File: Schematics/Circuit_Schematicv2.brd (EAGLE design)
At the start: 139.1 x 33.1 mm, 74 parts, among them Q2 LE33CZ

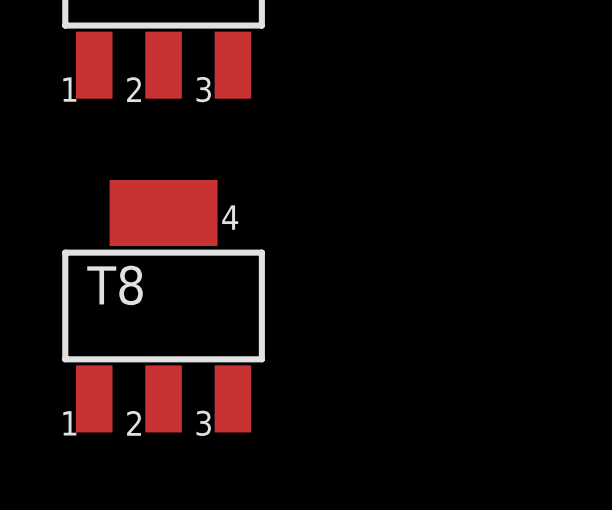
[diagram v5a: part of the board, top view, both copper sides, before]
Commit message: Final hardware changes and removed serial monitor from esp code in attempt to reduce noise
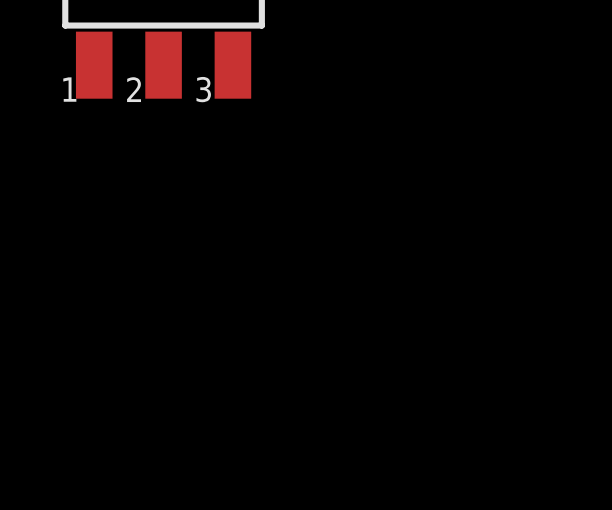
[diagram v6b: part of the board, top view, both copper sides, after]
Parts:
- removed T8: (no value), zetex:SOT223
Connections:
- removed net FAV3_GATE: MDL1.11, T8.1
- new net ESP_GPIO0: MDL1.12, R5.2, S2.2
- net FAV3: no longer T8.2, T8.4
- net GND: no longer T8.3
- net PREVIOUS_GATE: now also MDL1.11; no longer MDL1.12, R5.2, S2.2
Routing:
- net PREVIOUS_GATE: track 23.2 -> 0.00 mm, vias 2 -> 0
- net ESP_GPIO0: track 0.00 -> 23.2 mm, vias 0 -> 2
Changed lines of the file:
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@@
 <attribute name="OC_FARNELL" value="unknown" x="-85.8266" y="-64.135" size="1.778" layer="27" display="off"/>
-</element>
-<element name="T8" library="zetex" package="SOT223" value="" x="-85.8266" y="-75.2602">
-<attribute name="MF" value="" x="-85.8266" y="-75.2602" size="1.778" layer="27" display="off"/>
-<attribute name="OC_NEWARK" value="unknown" x="-85.8266" y="-75.2602" size="1.778" layer="27" display="off"/>
-<attribute name="MPN" value="" x="-85.8266" y="-75.2602" size="1.778" layer="27" display="off"/>
-<attribute name="OC_FARNELL" value="unknown" x="-85.8266" y="-75.2602" size="1.778" layer="27" display="off"/>
 </element>
 </elements>
@@
 <contactref element="T6" pad="3"/>
 <contactref element="T7" pad="3"/>
-<contactref element="T8" pad="3"/>
-<wire x1="-83.5152" y1="-67.2338" x2="-83.5152" y2="-78.359" width="0" layer="19" extent="1-1"/>
 <wire x1="-83.5152" y1="-56.1086" x2="-83.5152" y2="-67.2338" width="0" layer="19" extent="1-1"/>
 <wire x1="-83.5152" y1="-44.9834" x2="-83.5152" y2="-56.1086" width="0" layer="19" extent="1-1"/>
@@
 <wire x1="-2.3368" y1="25.527" x2="-1.524" y2="26.3398" width="0.2032" layer="16"/>
 <wire x1="-10.42035" y1="27.99715" x2="-11.7475" y2="26.67" width="0.2032" layer="1"/>
-<contactref element="T8" pad="4"/>
-<contactref element="T8" pad="2"/>
-<wire x1="-85.8266" y1="-72.1612" x2="-85.8266" y2="-78.359" width="0" layer="19" extent="1-1"/>
-<wire x1="-64.61125" y1="18.415" x2="-85.8266" y2="-72.1612" width="0" layer="19" extent="1-1"/>
 </signal>
 <signal name="FAV1">
@@
 <signal name="PREVIOUS_GATE">
 <contactref element="T2" pad="1"/>
+<contactref element="MDL1" pad="11"/>
+<wire x1="30.765" y1="28.25" x2="-88.138" y2="-11.6078" width="0" layer="19" extent="1-1"/>
+</signal>
+<signal name="VOLUP_GATE">
+<contactref element="T3" pad="1"/>
+<contactref element="MDL1" pad="14"/>
+<wire x1="36.765" y1="28.25" x2="-88.138" y2="-22.733" width="0" layer="19" extent="1-1"/>
+</signal>
+<signal name="VOLDOWN_GATE">
+<contactref element="T4" pad="1"/>
+<contactref element="MDL1" pad="13"/>
+<wire x1="34.765" y1="28.25" x2="-88.138" y2="-33.8582" width="0" layer="19" extent="1-1"/>
+</signal>
+<signal name="MUTE_GATE">
+<contactref element="T5" pad="1"/>
+<contactref element="MDL1" pad="5"/>
+<wire x1="32.765" y1="44.45" x2="-88.138" y2="-44.9834" width="0" layer="19" extent="1-1"/>
+</signal>
+<signal name="FAV1_GATE">
+<contactref element="T6" pad="1"/>
+<contactref element="MDL1" pad="4"/>
+<wire x1="34.765" y1="44.45" x2="-88.138" y2="-56.1086" width="0" layer="19" extent="1-1"/>
+</signal>
+<signal name="FAV2_GATE">
+<contactref element="T7" pad="1"/>
+<contactref element="MDL1" pad="7"/>
+<wire x1="28.765" y1="44.45" x2="-88.138" y2="-67.2338" width="0" layer="19" extent="1-1"/>
+</signal>
+<signal name="ESP_GPIO0">
 <contactref element="MDL1" pad="12"/>
 <contactref element="R5" pad="2"/>
@@
 <via x="32.86125" y="26.51125" extent="1-16" drill="0.6096"/>
 <via x="44.45" y="26.51125" extent="1-16" drill="0.6096"/>
-<wire x1="32.86125" y1="26.51125" x2="-88.138" y2="-11.6078" width="0" layer="19" extent="1-1"/>
-</signal>
-<signal name="VOLUP_GATE">
-<contactref element="T3" pad="1"/>
-<contactref element="MDL1" pad="14"/>
-<wire x1="36.765" y1="28.25" x2="-88.138" y2="-22.733" width="0" layer="19" extent="1-1"/>
-</signal>
-<signal name="VOLDOWN_GATE">
-<contactref element="T4" pad="1"/>
-<contactref element="MDL1" pad="13"/>
-<wire x1="34.765" y1="28.25" x2="-88.138" y2="-33.8582" width="0" layer="19" extent="1-1"/>
-</signal>
-<signal name="MUTE_GATE">
-<contactref element="T5" pad="1"/>
-<contactref element="MDL1" pad="5"/>
-<wire x1="32.765" y1="44.45" x2="-88.138" y2="-44.9834" width="0" layer="19" extent="1-1"/>
-</signal>
-<signal name="FAV1_GATE">
-<contactref element="T6" pad="1"/>
-<contactref element="MDL1" pad="4"/>
-<wire x1="34.765" y1="44.45" x2="-88.138" y2="-56.1086" width="0" layer="19" extent="1-1"/>
-</signal>
-<signal name="FAV2_GATE">
-<contactref element="T7" pad="1"/>
-<contactref element="MDL1" pad="7"/>
-<wire x1="28.765" y1="44.45" x2="-88.138" y2="-67.2338" width="0" layer="19" extent="1-1"/>
-</signal>
-<signal name="FAV3_GATE">
-<contactref element="T8" pad="1"/>
-<contactref element="MDL1" pad="11"/>
-<wire x1="30.765" y1="28.25" x2="-88.138" y2="-78.359" width="0" layer="19" extent="1-1"/>
 </signal>
 </signals>

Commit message: Updated the PS for the PIC
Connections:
- removed net N$1: U$1.19, U$1.57
- net 3.3V: now also U$1.19, U$1.57
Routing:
- net N$1: track 13.2 -> 0.00 mm
- net 3.3V: track 279.1 -> 292.3 mm
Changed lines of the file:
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@@
 <?xml version="1.0" encoding="utf-8"?>
 <!DOCTYPE eagle SYSTEM "eagle.dtd">
-<eagle version="8.0.0">
+<eagle version="8.1.0">
 <drawing>
 <settings>
@@
 <element name="T1" library="zetex" package="SOT223" value="" x="-85.8266" y="2.6162">
 <attribute name="MF" value="" x="-85.8266" y="2.6162" size="1.778" layer="27" display="off"/>
-<attribute name="OC_NEWARK" value="unknown" x="-85.8266" y="2.6162" size="1.778" layer="27" display="off"/>
 <attribute name="MPN" value="" x="-85.8266" y="2.6162" size="1.778" layer="27" display="off"/>
 <attribute name="OC_FARNELL" value="unknown" x="-85.8266" y="2.6162" size="1.778" layer="27" display="off"/>
+<attribute name="OC_NEWARK" value="unknown" x="-85.8266" y="2.6162" size="1.778" layer="27" display="off"/>
 </element>
 <element name="T2" library="zetex" package="SOT223" value="" x="-85.8266" y="-8.509">
 <attribute name="MF" value="" x="-85.8266" y="-8.509" size="1.778" layer="27" display="off"/>
-<attribute name="OC_NEWARK" value="unknown" x="-85.8266" y="-8.509" size="1.778" layer="27" display="off"/>
 <attribute name="MPN" value="" x="-85.8266" y="-8.509" size="1.778" layer="27" display="off"/>
 <attribute name="OC_FARNELL" value="unknown" x="-85.8266" y="-8.509" size="1.778" layer="27" display="off"/>
+<attribute name="OC_NEWARK" value="unknown" x="-85.8266" y="-8.509" size="1.778" layer="27" display="off"/>
 </element>
 <element name="T3" library="zetex" package="SOT223" value="" x="-85.8266" y="-19.6342">
 <attribute name="MF" value="" x="-85.8266" y="-19.6342" size="1.778" layer="27" display="off"/>
-<attribute name="OC_NEWARK" value="unknown" x="-85.8266" y="-19.6342" size="1.778" layer="27" display="off"/>
 <attribute name="MPN" value="" x="-85.8266" y="-19.6342" size="1.778" layer="27" display="off"/>
 <attribute name="OC_FARNELL" value="unknown" x="-85.8266" y="-19.6342" size="1.778" layer="27" display="off"/>
+<attribute name="OC_NEWARK" value="unknown" x="-85.8266" y="-19.6342" size="1.778" layer="27" display="off"/>
 </element>
 <element name="T4" library="zetex" package="SOT223" value="" x="-85.8266" y="-30.7594">
 <attribute name="MF" value="" x="-85.8266" y="-30.7594" size="1.778" layer="27" display="off"/>
-<attribute name="OC_NEWARK" value="unknown" x="-85.8266" y="-30.7594" size="1.778" layer="27" display="off"/>
 <attribute name="MPN" value="" x="-85.8266" y="-30.7594" size="1.778" layer="27" display="off"/>
 <attribute name="OC_FARNELL" value="unknown" x="-85.8266" y="-30.7594" size="1.778" layer="27" display="off"/>
+<attribute name="OC_NEWARK" value="unknown" x="-85.8266" y="-30.7594" size="1.778" layer="27" display="off"/>
 </element>
 <element name="T5" library="zetex" package="SOT223" value="" x="-85.8266" y="-41.8846">
 <attribute name="MF" value="" x="-85.8266" y="-41.8846" size="1.778" layer="27" display="off"/>
-<attribute name="OC_NEWARK" value="unknown" x="-85.8266" y="-41.8846" size="1.778" layer="27" display="off"/>
 <attribute name="MPN" value="" x="-85.8266" y="-41.8846" size="1.778" layer="27" display="off"/>
 <attribute name="OC_FARNELL" value="unknown" x="-85.8266" y="-41.8846" size="1.778" layer="27" display="off"/>
+<attribute name="OC_NEWARK" value="unknown" x="-85.8266" y="-41.8846" size="1.778" layer="27" display="off"/>
 </element>
 <element name="T6" library="zetex" package="SOT223" value="" x="-85.8266" y="-53.0098">
 <attribute name="MF" value="" x="-85.8266" y="-53.0098" size="1.778" layer="27" display="off"/>
-<attribute name="OC_NEWARK" value="unknown" x="-85.8266" y="-53.0098" size="1.778" layer="27" display="off"/>
 <attribute name="MPN" value="" x="-85.8266" y="-53.0098" size="1.778" layer="27" display="off"/>
 <attribute name="OC_FARNELL" value="unknown" x="-85.8266" y="-53.0098" size="1.778" layer="27" display="off"/>
+<attribute name="OC_NEWARK" value="unknown" x="-85.8266" y="-53.0098" size="1.778" layer="27" display="off"/>
 </element>
 <element name="T7" library="zetex" package="SOT223" value="" x="-85.8266" y="-64.135">
 <attribute name="MF" value="" x="-85.8266" y="-64.135" size="1.778" layer="27" display="off"/>
-<attribute name="OC_NEWARK" value="unknown" x="-85.8266" y="-64.135" size="1.778" layer="27" display="off"/>
 <attribute name="MPN" value="" x="-85.8266" y="-64.135" size="1.778" layer="27" display="off"/>
 <attribute name="OC_FARNELL" value="unknown" x="-85.8266" y="-64.135" size="1.778" layer="27" display="off"/>
+<attribute name="OC_NEWARK" value="unknown" x="-85.8266" y="-64.135" size="1.778" layer="27" display="off"/>
 </element>
 </elements>
@@
 <wire x1="-10.6426" y1="23.6982" x2="-12.6746" y2="23.6982" width="0.2032" layer="16"/>
 <wire x1="-12.6746" y1="23.6982" x2="-12.7" y2="23.6728" width="0.2032" layer="16"/>
+<contactref element="U$1" pad="57"/>
+<contactref element="U$1" pad="19"/>
+<wire x1="-14.097" y1="40.9956" x2="-14.097" y2="41.6814" width="0.2032" layer="1"/>
+<wire x1="-16.5862" y1="31.9024" x2="-16.5862" y2="30.2006" width="0.2032" layer="1"/>
+<wire x1="-14.097" y1="41.6814" x2="-14.097" y2="40.6146" width="0.2032" layer="1"/>
+<wire x1="-14.097" y1="40.6146" x2="-14.5796" y2="40.132" width="0.2032" layer="1"/>
+<wire x1="-14.5796" y1="40.132" x2="-14.5796" y2="36.6014" width="0.2032" layer="1"/>
+<wire x1="-14.5796" y1="36.6014" x2="-14.986" y2="36.195" width="0.2032" layer="1"/>
+<wire x1="-14.986" y1="36.195" x2="-14.986" y2="33.5026" width="0.2032" layer="1"/>
+<wire x1="-14.986" y1="33.5026" x2="-16.5862" y2="31.9024" width="0.2032" layer="1"/>
+<wire x1="-13.081" y1="30.2006" x2="-16.5862" y2="30.2006" width="0" layer="19" extent="1-1"/>
 </signal>
 <signal name="L-OUT">
@@
 <contactref element="U$1" pad="41"/>
 </signal>
-<signal name="N$1">
-<contactref element="U$1" pad="57"/>
-<contactref element="U$1" pad="19"/>
-<wire x1="-14.097" y1="40.9956" x2="-14.097" y2="41.6814" width="0.2032" layer="1"/>
-<wire x1="-16.5862" y1="31.9024" x2="-16.5862" y2="30.2006" width="0.2032" layer="1"/>
-<wire x1="-14.097" y1="41.6814" x2="-14.097" y2="40.6146" width="0.2032" layer="1"/>
-<wire x1="-14.097" y1="40.6146" x2="-14.5796" y2="40.132" width="0.2032" layer="1"/>
-<wire x1="-14.5796" y1="40.132" x2="-14.5796" y2="36.6014" width="0.2032" layer="1"/>
-<wire x1="-14.5796" y1="36.6014" x2="-14.986" y2="36.195" width="0.2032" layer="1"/>
-<wire x1="-14.986" y1="36.195" x2="-14.986" y2="33.5026" width="0.2032" layer="1"/>
-<wire x1="-14.986" y1="33.5026" x2="-16.5862" y2="31.9024" width="0.2032" layer="1"/>
-</signal>
 <signal name="VDD_4">

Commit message: removed some circuit confusions
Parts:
- removed R15: 10k, SparkFun-Resistors:0603
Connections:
- removed net ENABLE: R15.2
- removed net N$51: JP2.2, VR1.2
- new net VDD_2: U$1.26
- net 3.3V: now also JP2.2; no longer R15.1, U$1.26
- net VO: now also VR1.2
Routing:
- net N$51: track 99.1 -> 0.00 mm
- net VO: track 0.00 -> 95.3 mm
- net ENABLE: track 65.6 -> 0.00 mm, vias 5 -> 0
- net 3.3V: track 292.3 -> 286.0 mm
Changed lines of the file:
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@@
 <?xml version="1.0" encoding="utf-8"?>
 <!DOCTYPE eagle SYSTEM "eagle.dtd">
-<eagle version="8.1.0">
+<eagle version="7.7.0">
 <drawing>
 <settings>
@@
 <attribute name="PROD_ID" value="RES-00824" x="-53.086" y="31.877" size="1.778" layer="28" rot="MR270" display="off"/>
 </element>
-<element name="R15" library="SparkFun-Resistors" package="0603" value="10k" x="-25.908" y="32.512" rot="MR180">
-<attribute name="PROD_ID" value="RES-00824" x="-25.908" y="32.512" size="1.778" layer="28" rot="MR180" display="off"/>
-</element>
 <element name="R2" library="SparkFun-Resistors" package="0603" value="10k" x="-25.908" y="40.513" rot="MR180">
 <attribute name="PROD_ID" value="RES-00824" x="-25.908" y="40.513" size="1.778" layer="28" rot="MR180" display="off"/>
@@
 <contactref element="MDL1" pad="8"/>
 <contactref element="U$4" pad="VCC"/>
-<contactref element="U$1" pad="26"/>
 <contactref element="R5" pad="1"/>
 <contactref element="VR1" pad="1"/>
@@
 <contactref element="R11" pad="2"/>
 <contactref element="R2" pad="2"/>
-<contactref element="R15" pad="1"/>
 <contactref element="R17" pad="1"/>
 <contactref element="R16" pad="1"/>
 <wire x1="-25.0825" y1="34.13125" x2="-26.67" y2="32.54375" width="0.2032" layer="16"/>
 <wire x1="-25.0825" y1="36.67125" x2="-25.0825" y2="34.13125" width="0.2032" layer="16"/>
-<wire x1="-26.67" y1="32.54375" x2="-26.758" y2="32.512" width="0.2032" layer="16"/>
 <wire x1="-25.0825" y1="36.67125" x2="-25.058" y2="36.703" width="0.2032" layer="16"/>
 <wire x1="-53.18125" y1="32.86125" x2="-54.76875" y2="32.86125" width="0.2032" layer="16"/>
@@
 <wire x1="-41.5925" y1="32.7025" x2="-41.529" y2="32.6" width="0.2032" layer="16"/>
 <wire x1="-38.735" y1="32.54375" x2="-26.82875" y2="32.54375" width="0.2032" layer="16"/>
-<wire x1="-26.82875" y1="32.54375" x2="-26.758" y2="32.512" width="0.2032" layer="16"/>
 <wire x1="-38.735" y1="32.54375" x2="-38.862" y2="32.6" width="0.2032" layer="16"/>
 <wire x1="-20.6375" y1="45.72" x2="-20.6375" y2="48.895" width="0.2032" layer="1"/>
@@
 <via x="1.27" y="20.6375" extent="1-16" drill="0.6096"/>
 <via x="-62.07125" y="29.05125" extent="1-16" drill="0.6096"/>
-<wire x1="-13.081" y1="30.2006" x2="-13.081" y2="24.0792" width="0.2032" layer="1"/>
 <wire x1="-12.6746" y1="23.6728" x2="-13.081" y2="24.0792" width="0.2032" layer="1"/>
 <via x="-10.6426" y="23.6982" extent="1-16" drill="0.6" diameter="0.4064"/>
@@
 <wire x1="-14.986" y1="36.195" x2="-14.986" y2="33.5026" width="0.2032" layer="1"/>
 <wire x1="-14.986" y1="33.5026" x2="-16.5862" y2="31.9024" width="0.2032" layer="1"/>
-<wire x1="-13.081" y1="30.2006" x2="-16.5862" y2="30.2006" width="0" layer="19" extent="1-1"/>
+<contactref element="JP2" pad="2"/>
+<wire x1="26.765" y1="44.45" x2="44.45" y2="47.625" width="0" layer="19" extent="1-1"/>
+<wire x1="-26.67" y1="32.54375" x2="-26.82875" y2="32.54375" width="0" layer="19" extent="16-16"/>
+<wire x1="-16.5862" y1="30.2006" x2="-13.081" y2="24.0792" width="0" layer="19" extent="1-1"/>
 </signal>
 <signal name="L-OUT">
@@
 <wire x1="-29.0068" y1="28.6766" x2="-85.8266" y2="-27.6604" width="0" layer="19" extent="1-1"/>
 </signal>
-<signal name="ENABLE">
-<contactref element="R15" pad="2"/>
-<wire x1="-21.74875" y1="35.71875" x2="-24.92375" y2="32.54375" width="0.2032" layer="16"/>
-<wire x1="-13.97" y1="35.71875" x2="-21.74875" y2="35.71875" width="0.2032" layer="16"/>
-<wire x1="-8.41375" y1="41.11625" x2="-12.85875" y2="41.11625" width="0.2032" layer="16"/>
-<wire x1="-6.82625" y1="42.70375" x2="-8.41375" y2="41.11625" width="0.2032" layer="1"/>
-<wire x1="31.59125" y1="42.70375" x2="-6.82625" y2="42.70375" width="0.2032" layer="16"/>
-<wire x1="31.59125" y1="43.18" x2="31.59125" y2="42.70375" width="0.2032" layer="1"/>
-<wire x1="32.86125" y1="44.45" x2="31.59125" y2="43.18" width="0.2032" layer="1"/>
-<wire x1="-24.92375" y1="32.54375" x2="-25.058" y2="32.512" width="0.2032" layer="16"/>
-<via x="-13.97" y="35.71875" extent="1-16" drill="0.6096"/>
-<via x="-13.5382" y="39.8018" extent="1-16" drill="0.6096"/>
-<via x="-8.41375" y="41.11625" extent="1-16" drill="0.6096"/>
-<via x="-6.82625" y="42.70375" extent="1-16" drill="0.6096"/>
-<via x="31.59125" y="42.70375" extent="1-16" drill="0.6096"/>
-<wire x1="-12.85875" y1="41.11625" x2="-12.85875" y2="40.48125" width="0.2032" layer="16"/>
-<wire x1="-12.85875" y1="40.48125" x2="-13.5382" y2="39.8018" width="0.2032" layer="16"/>
-<wire x1="-13.5382" y1="39.8018" x2="-13.5382" y2="36.15055" width="0.2032" layer="1"/>
-<wire x1="-13.5382" y1="36.15055" x2="-13.97" y2="35.71875" width="0.2032" layer="1"/>
-</signal>
 <signal name="DB4">
 <contactref element="U$1" pad="52"/>
@@
 <signal name="VO">
 <contactref element="JP2" pad="3"/>
+<contactref element="VR1" pad="2"/>
+<wire x1="-38.25875" y1="21.2725" x2="-36.23945" y2="22.7584" width="0.2032" layer="16"/>
+<wire x1="-14.8717" y1="22.9108" x2="-14.9225" y2="22.86" width="0.2032" layer="16"/>
+<wire x1="-14.8717" y1="22.9108" x2="-12.22375" y2="25.55875" width="0.2032" layer="16"/>
+<wire x1="24.92375" y1="28.2575" x2="25.7175" y2="28.2575" width="0.2032" layer="16"/>
+<wire x1="25.7175" y1="28.2575" x2="41.75125" y2="44.29125" width="0.2032" layer="16"/>
+<wire x1="-38.25875" y1="21.2725" x2="-38.378" y2="21.209" width="0.2032" layer="16"/>
+<wire x1="-12.22375" y1="25.55875" x2="-6.96595" y2="25.55875" width="0.2032" layer="16"/>
+<wire x1="-6.96595" y1="25.55875" x2="-5.7658" y2="24.3586" width="0.2032" layer="16"/>
+<wire x1="-5.7658" y1="24.3586" x2="-1.651" y2="24.3586" width="0.2032" layer="16"/>
+<wire x1="-1.651" y1="24.3586" x2="-0.7112" y2="25.2984" width="0.2032" layer="16"/>
+<wire x1="-0.7112" y1="25.2984" x2="2.3114" y2="25.2984" width="0.2032" layer="16"/>
+<wire x1="2.3114" y1="25.2984" x2="7.112" y2="20.4978" width="0.2032" layer="16"/>
+<wire x1="7.112" y1="20.4978" x2="11.557" y2="20.4978" width="0.2032" layer="16"/>
+<wire x1="11.557" y1="20.4978" x2="11.5824" y2="20.4724" width="0.2032" layer="16"/>
+<wire x1="11.5824" y1="20.4724" x2="11.6078" y2="20.4724" width="0.2032" layer="16"/>
+<wire x1="11.6078" y1="20.4724" x2="14.8336" y2="23.6982" width="0.2032" layer="16"/>
+<wire x1="14.8336" y1="23.6982" x2="18.9738" y2="23.6982" width="0.2032" layer="16"/>
+<wire x1="18.9738" y1="23.6982" x2="20.828" y2="25.5524" width="0.2032" layer="16"/>
+<wire x1="20.828" y1="25.5524" x2="22.21865" y2="25.5524" width="0.2032" layer="16"/>
+<wire x1="22.21865" y1="25.5524" x2="24.92375" y2="28.2575" width="0.2032" layer="16"/>
+<wire x1="-36.23945" y1="22.7584" x2="-35.3314" y2="22.7584" width="0.2032" layer="16"/>
+<wire x1="-35.3314" y1="22.7584" x2="-35.179" y2="22.9108" width="0.2032" layer="16"/>
+<wire x1="-35.179" y1="22.9108" x2="-14.8717" y2="22.9108" width="0.2032" layer="16"/>
+<wire x1="41.75125" y1="44.29125" x2="41.75125" y2="44.92625" width="0.2032" layer="16"/>
+<wire x1="41.75125" y1="44.92625" x2="41.91" y2="47.625" width="0" layer="19" extent="16-16"/>
 </signal>
 <signal name="RS">
@@
 <wire x1="-45.72" y1="41.75125" x2="-45.7708" y2="41.783" width="0.2032" layer="16"/>
 </signal>
-<signal name="N$51">
-<contactref element="JP2" pad="2"/>
-<contactref element="VR1" pad="2"/>
-<wire x1="-38.25875" y1="21.2725" x2="-36.23945" y2="22.7584" width="0.2032" layer="16"/>
-<wire x1="-14.8717" y1="22.9108" x2="-14.9225" y2="22.86" width="0.2032" layer="16"/>
-<wire x1="-14.8717" y1="22.9108" x2="-12.22375" y2="25.55875" width="0.2032" layer="16"/>
-<wire x1="24.92375" y1="28.2575" x2="25.7175" y2="28.2575" width="0.2032" layer="16"/>
-<wire x1="25.7175" y1="28.2575" x2="41.75125" y2="44.29125" width="0.2032" layer="16"/>
-<wire x1="-38.25875" y1="21.2725" x2="-38.378" y2="21.209" width="0.2032" layer="16"/>
-<wire x1="-12.22375" y1="25.55875" x2="-6.96595" y2="25.55875" width="0.2032" layer="16"/>
-<wire x1="-6.96595" y1="25.55875" x2="-5.7658" y2="24.3586" width="0.2032" layer="16"/>
-<wire x1="-5.7658" y1="24.3586" x2="-1.651" y2="24.3586" width="0.2032" layer="16"/>
-<wire x1="-1.651" y1="24.3586" x2="-0.7112" y2="25.2984" width="0.2032" layer="16"/>
-<wire x1="-0.7112" y1="25.2984" x2="2.3114" y2="25.2984" width="0.2032" layer="16"/>
-<wire x1="2.3114" y1="25.2984" x2="7.112" y2="20.4978" width="0.2032" layer="16"/>
-<wire x1="7.112" y1="20.4978" x2="11.557" y2="20.4978" width="0.2032" layer="16"/>
-<wire x1="11.557" y1="20.4978" x2="11.5824" y2="20.4724" width="0.2032" layer="16"/>
-<wire x1="11.5824" y1="20.4724" x2="11.6078" y2="20.4724" width="0.2032" layer="16"/>
-<wire x1="11.6078" y1="20.4724" x2="14.8336" y2="23.6982" width="0.2032" layer="16"/>
-<wire x1="14.8336" y1="23.6982" x2="18.9738" y2="23.6982" width="0.2032" layer="16"/>
-<wire x1="18.9738" y1="23.6982" x2="20.828" y2="25.5524" width="0.2032" layer="16"/>
-<wire x1="20.828" y1="25.5524" x2="22.21865" y2="25.5524" width="0.2032" layer="16"/>
-<wire x1="22.21865" y1="25.5524" x2="24.92375" y2="28.2575" width="0.2032" layer="16"/>
-<wire x1="-36.23945" y1="22.7584" x2="-35.3314" y2="22.7584" width="0.2032" layer="16"/>
-<wire x1="-35.3314" y1="22.7584" x2="-35.179" y2="22.9108" width="0.2032" layer="16"/>
-<wire x1="-35.179" y1="22.9108" x2="-14.8717" y2="22.9108" width="0.2032" layer="16"/>
-<wire x1="41.75125" y1="44.29125" x2="41.75125" y2="44.92625" width="0.2032" layer="16"/>
-<wire x1="41.75125" y1="44.92625" x2="44.45" y2="47.625" width="0.2032" layer="16"/>
-</signal>
 <signal name="VSS_4">
 <contactref element="U$1" pad="25"/>
@@
 <via x="44.45" y="26.51125" extent="1-16" drill="0.6096"/>
 </signal>
+<signal name="VDD_2">
+<contactref element="U$1" pad="26"/>
+</signal>
 </signals>
